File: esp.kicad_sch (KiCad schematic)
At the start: 26 parts, among them J1 Barrel_Jack, J3 Barrel_Jack, J4 Barrel_Jack, J5 Barrel_Jack, J7 Barrel_Jack_MountingPin, P1 Conn_WallPlug_Earth, U1 ESP32-S2-WROVER, U14 PCF8574ATS, U16 L298N, U17 PCA9685PW, U18 NID30S48-24, U2 TCA9548ARGER, U3 TCA9548ARGER, U4 BME280, U5 CCS811, U6 PCF8574ATS, U7 OKI-78SR-12_1.0-W36H-C, U8 OKI-78SR-5_1.5-W36-C, U9 OKI-78SR-3.3_1.5-W36H-C

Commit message: motor layout
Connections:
- net GND: no longer U3.9 (GND)
- net at U3.22 (A0): no longer U3.23 (A1)
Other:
- moved on the sheet: U14, U17, U3, U6
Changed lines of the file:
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@@
   (junction (at 66.04 30.48) (diameter 0) (color 0 0 0 0)
   )
-  (junction (at 44.45 88.9) (diameter 0) (color 0 0 0 0)
-  )
   (junction (at 267.97 60.96) (diameter 0) (color 0 0 0 0)
   )
@@
     (stroke (width 0) (type default))
   )
-  (wire (pts (xy 82.55 62.23) (xy 85.09 62.23))
-    (stroke (width 0) (type default))
-  )
   (wire (pts (xy 196.85 24.13) (xy 196.85 36.83))
     (stroke (width 0) (type default))
@@
     (stroke (width 0) (type default))
   )
-  (wire (pts (xy 31.75 88.9) (xy 31.75 102.87))
-    (stroke (width 0) (type default))
-  )
-  (wire (pts (xy 31.75 88.9) (xy 44.45 88.9))
-    (stroke (width 0) (type default))
-  )
   (wire (pts (xy 31.75 168.91) (xy 25.4 168.91))
     (stroke (width 0) (type default))
@@
     (stroke (width 0) (type default))
   )
-  (wire (pts (xy 69.85 72.39) (xy 44.45 72.39))
-    (stroke (width 0) (type default))
-  )
   (wire (pts (xy 162.56 50.8) (xy 173.99 50.8))
     (stroke (width 0) (type default))
@@
     (stroke (width 0) (type default))
   )
-  (wire (pts (xy 44.45 72.39) (xy 44.45 88.9))
-    (stroke (width 0) (type default))
-  )
   (wire (pts (xy 267.97 71.12) (xy 267.97 78.74))
     (stroke (width 0) (type default))
@@
     (stroke (width 0) (type default))
   )
-  (wire (pts (xy 110.49 62.23) (xy 110.49 54.61))
-    (stroke (width 0) (type default))
-  )
   (wire (pts (xy 27.94 25.4) (xy 33.02 25.4))
     (stroke (width 0) (type default))
@@
   )
   (wire (pts (xy 53.34 25.4) (xy 54.61 25.4))
-    (stroke (width 0) (type default))
-  )
-  (wire (pts (xy 113.03 62.23) (xy 113.03 57.15))
     (stroke (width 0) (type default))
   )
@@
     )
   )
-  (symbol (lib_id "Driver_LED:PCA9685PW") (at 99.06 132.08 180) (unit 1)
-    (in_bom yes) (on_board yes) (dnp no) (fields_autoplaced)
-    (property "Reference" "U17" (at 99.4059 104.14 0)
-      (effects (font (size 1.27 1.27)) (justify right))
-    )
-    (property "Value" "PCA9685PW" (at 99.4059 106.68 0)
-      (effects (font (size 1.27 1.27)) (justify right))
-    )
-    (property "Footprint" "Package_SO:TSSOP-28_4.4x9.7mm_P0.65mm" (at 98.425 107.315 0)
+  (symbol (lib_id "Driver_LED:PCA9685PW") (at 123.19 146.05 180) (unit 1)
+    (in_bom yes) (on_board yes) (dnp no) (fields_autoplaced)
+    (property "Reference" "U17" (at 123.5359 118.11 0)
+      (effects (font (size 1.27 1.27)) (justify right))
+    )
+    (property "Value" "PCA9685PW" (at 123.5359 120.65 0)
+      (effects (font (size 1.27 1.27)) (justify right))
+    )
+    (property "Footprint" "Package_SO:TSSOP-28_4.4x9.7mm_P0.65mm" (at 122.555 121.285 0)
       (effects (font (size 1.27 1.27)) (justify left) hide)
     )
-    (property "Datasheet" "http://www.nxp.com/docs/en/data-sheet/PCA9685.pdf" (at 109.22 149.86 0)
+    (property "Datasheet" "http://www.nxp.com/docs/en/data-sheet/PCA9685.pdf" (at 133.35 163.83 0)
       (effects (font (size 1.27 1.27)) hide)
     )
@@
     )
   )
-  (symbol (lib_id "Interface_Expansion:TCA9548ARGER") (at 95.25 72.39 270) (unit 1)
-    (in_bom yes) (on_board yes) (dnp no) (fields_autoplaced)
-    (property "Reference" "U3" (at 124.46 65.4619 90)
-      (effects (font (size 1.27 1.27)))
-    )
-    (property "Value" "TCA9548ARGER" (at 124.46 68.0019 90)
-      (effects (font (size 1.27 1.27)))
-    )
-    (property "Footprint" "Package_DFN_QFN:Texas_RGE0024C_EP2.1x2.1mm" (at 69.85 72.39 0)
-      (effects (font (size 1.27 1.27)) hide)
-    )
-    (property "Datasheet" "http://www.ti.com/lit/ds/symlink/tca9548a.pdf" (at 101.6 73.66 0)
+  (symbol (lib_id "Interface_Expansion:TCA9548ARGER") (at 162.56 138.43 180) (unit 1)
+    (in_bom yes) (on_board yes) (dnp no) (fields_autoplaced)
+    (property "Reference" "U3" (at 162.9059 110.49 0)
+      (effects (font (size 1.27 1.27)) (justify right))
+    )
+    (property "Value" "TCA9548ARGER" (at 162.9059 113.03 0)
+      (effects (font (size 1.27 1.27)) (justify right))
+    )
+    (property "Footprint" "Package_DFN_QFN:Texas_RGE0024C_EP2.1x2.1mm" (at 162.56 113.03 0)
+      (effects (font (size 1.27 1.27)) hide)
+    )
+    (property "Datasheet" "http://www.ti.com/lit/ds/symlink/tca9548a.pdf" (at 161.29 144.78 0)
       (effects (font (size 1.27 1.27)) hide)
     )
@@
     )
   )
-  (symbol (lib_id "power:GND") (at 44.45 88.9 0) (unit 1)
-    (in_bom yes) (on_board yes) (dnp no) (fields_autoplaced)
-    (property "Reference" "#PWR02" (at 44.45 95.25 0)
-      (effects (font (size 1.27 1.27)) hide)
-    )
-    (property "Value" "GND" (at 44.45 93.98 0)
-      (effects (font (size 1.27 1.27)))
-    )
-    (property "Footprint" "" (at 44.45 88.9 0)
-      (effects (font (size 1.27 1.27)) hide)
-    )
-    (property "Datasheet" "" (at 44.45 88.9 0)
-      (effects (font (size 1.27 1.27)) hide)
-    )
-    (pin "1")
-    (instances
-      (project "esp"
-        (path "/dab6683c-420f-459a-bf9c-0c28b4b081e3"
-          (reference "#PWR02") (unit 1)
-        )
-      )
-    )
-  )
   (symbol (lib_id "Connector:Conn_WallPlug_Earth") (at 20.32 27.94 0) (unit 1)
     (in_bom yes) (on_board yes) (dnp no) (fields_autoplaced)
@@
     )
   )
-  (symbol (lib_id "Interface_Expansion:PCF8574ATS") (at 100.33 179.07 180) (unit 1)
-    (in_bom yes) (on_board yes) (dnp no) (fields_autoplaced)
-    (property "Reference" "U6" (at 100.6759 158.75 0)
-      (effects (font (size 1.27 1.27)) (justify right))
-    )
-    (property "Value" "PCF8574ATS" (at 100.6759 161.29 0)
-      (effects (font (size 1.27 1.27)) (justify right))
-    )
-    (property "Footprint" "Package_SO:SSOP-20_4.4x6.5mm_P0.65mm" (at 100.33 179.07 0)
-      (effects (font (size 1.27 1.27)) hide)
-    )
-    (property "Datasheet" "http://www.nxp.com/docs/en/data-sheet/PCF8574_PCF8574A.pdf" (at 100.33 179.07 0)
+  (symbol (lib_id "Interface_Expansion:PCF8574ATS") (at 90.17 172.72 180) (unit 1)
+    (in_bom yes) (on_board yes) (dnp no) (fields_autoplaced)
+    (property "Reference" "U6" (at 90.5159 152.4 0)
+      (effects (font (size 1.27 1.27)) (justify right))
+    )
+    (property "Value" "PCF8574ATS" (at 90.5159 154.94 0)
+      (effects (font (size 1.27 1.27)) (justify right))
+    )
+    (property "Footprint" "Package_SO:SSOP-20_4.4x6.5mm_P0.65mm" (at 90.17 172.72 0)
+      (effects (font (size 1.27 1.27)) hide)
+    )
+    (property "Datasheet" "http://www.nxp.com/docs/en/data-sheet/PCF8574_PCF8574A.pdf" (at 90.17 172.72 0)
       (effects (font (size 1.27 1.27)) hide)
     )
@@
     )
   )
-  (symbol (lib_id "Interface_Expansion:PCF8574ATS") (at 63.5 106.68 180) (unit 1)
-    (in_bom yes) (on_board yes) (dnp no) (fields_autoplaced)
-    (property "Reference" "U14" (at 63.8459 86.36 0)
-      (effects (font (size 1.27 1.27)) (justify right))
-    )
-    (property "Value" "PCF8574ATS" (at 63.8459 88.9 0)
-      (effects (font (size 1.27 1.27)) (justify right))
-    )
-    (property "Footprint" "Package_SO:SSOP-20_4.4x6.5mm_P0.65mm" (at 63.5 106.68 0)
-      (effects (font (size 1.27 1.27)) hide)
-    )
-    (property "Datasheet" "http://www.nxp.com/docs/en/data-sheet/PCF8574_PCF8574A.pdf" (at 63.5 106.68 0)
+  (symbol (lib_id "Interface_Expansion:PCF8574ATS") (at 60.96 121.92 180) (unit 1)
+    (in_bom yes) (on_board yes) (dnp no) (fields_autoplaced)
+    (property "Reference" "U14" (at 61.3059 101.6 0)
+      (effects (font (size 1.27 1.27)) (justify right))
+    )
+    (property "Value" "PCF8574ATS" (at 61.3059 104.14 0)
+      (effects (font (size 1.27 1.27)) (justify right))
+    )
+    (property "Footprint" "Package_SO:SSOP-20_4.4x6.5mm_P0.65mm" (at 60.96 121.92 0)
+      (effects (font (size 1.27 1.27)) hide)
+    )
+    (property "Datasheet" "http://www.nxp.com/docs/en/data-sheet/PCF8574_PCF8574A.pdf" (at 60.96 121.92 0)
       (effects (font (size 1.27 1.27)) hide)
     )
@@
     )
   )
-  (sheet (at 12.7 148.59) (size 40.64 38.1) (fields_autoplaced)
+  (sheet (at 12.7 148.59) (size 149.86 48.26) (fields_autoplaced)
     (stroke (width 0.1524) (type solid))
     (fill (color 0 0 0 0.0000))
@@
       (effects (font (size 1.27 1.27)) (justify left bottom))
     )
-    (property "Sheetfile" "Barrel_Jack_Large_Motor.kicad_sch" (at 12.7 187.2746 0)
+    (property "Sheetfile" "Barrel_Jack_Large_Motor.kicad_sch" (at 12.7 197.4346 0)
       (effects (font (size 1.27 1.27)) (justify left top))
     )
@@
     )
   )
-  (sheet (at 19.05 104.14) (size 26.67 35.56) (fields_autoplaced)
+  (sheet (at 17.78 99.06) (size 144.78 44.45) (fields_autoplaced)
     (stroke (width 0.1524) (type solid))
     (fill (color 0 0 0 0.0000))
-    (property "Sheetname" "Barrel_Jack" (at 19.05 103.4284 0)
+    (property "Sheetname" "Barrel_Jack" (at 17.78 98.3484 0)
       (effects (font (size 1.27 1.27)) (justify left bottom))
     )
-    (property "Sheetfile" "Barrel_Jack.kicad_sch" (at 19.05 140.2846 0)
+    (property "Sheetfile" "Barrel_Jack.kicad_sch" (at 17.78 144.0946 0)
       (effects (font (size 1.27 1.27)) (justify left top))
     )

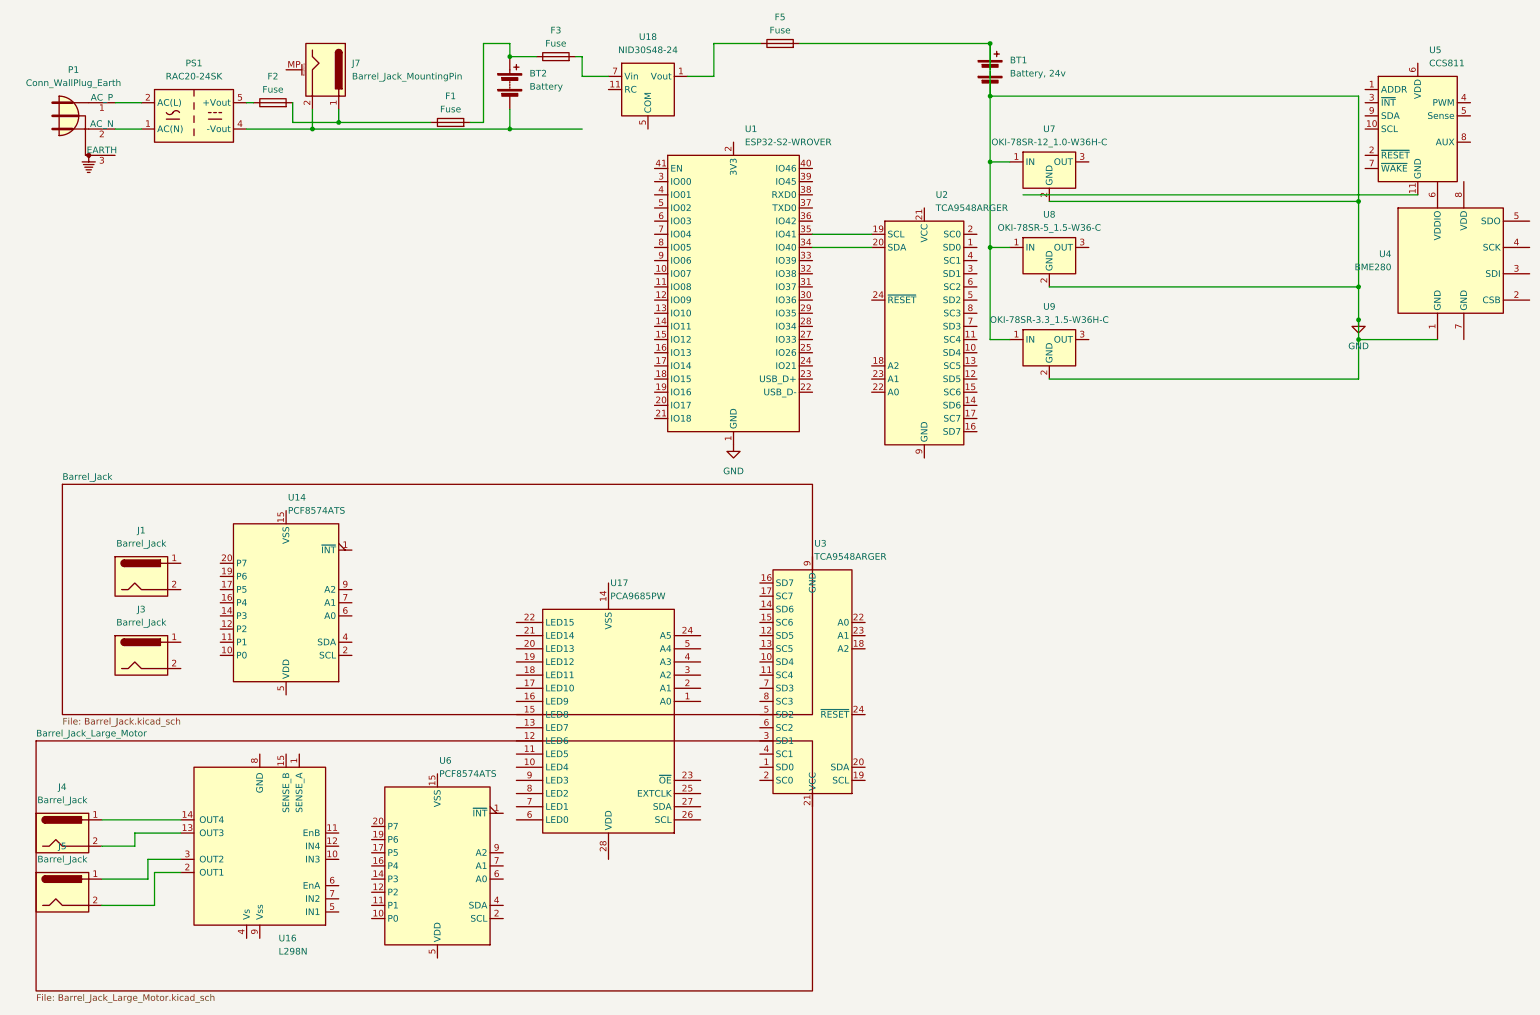
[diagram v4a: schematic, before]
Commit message: placeholders for ethernet and relay inputs
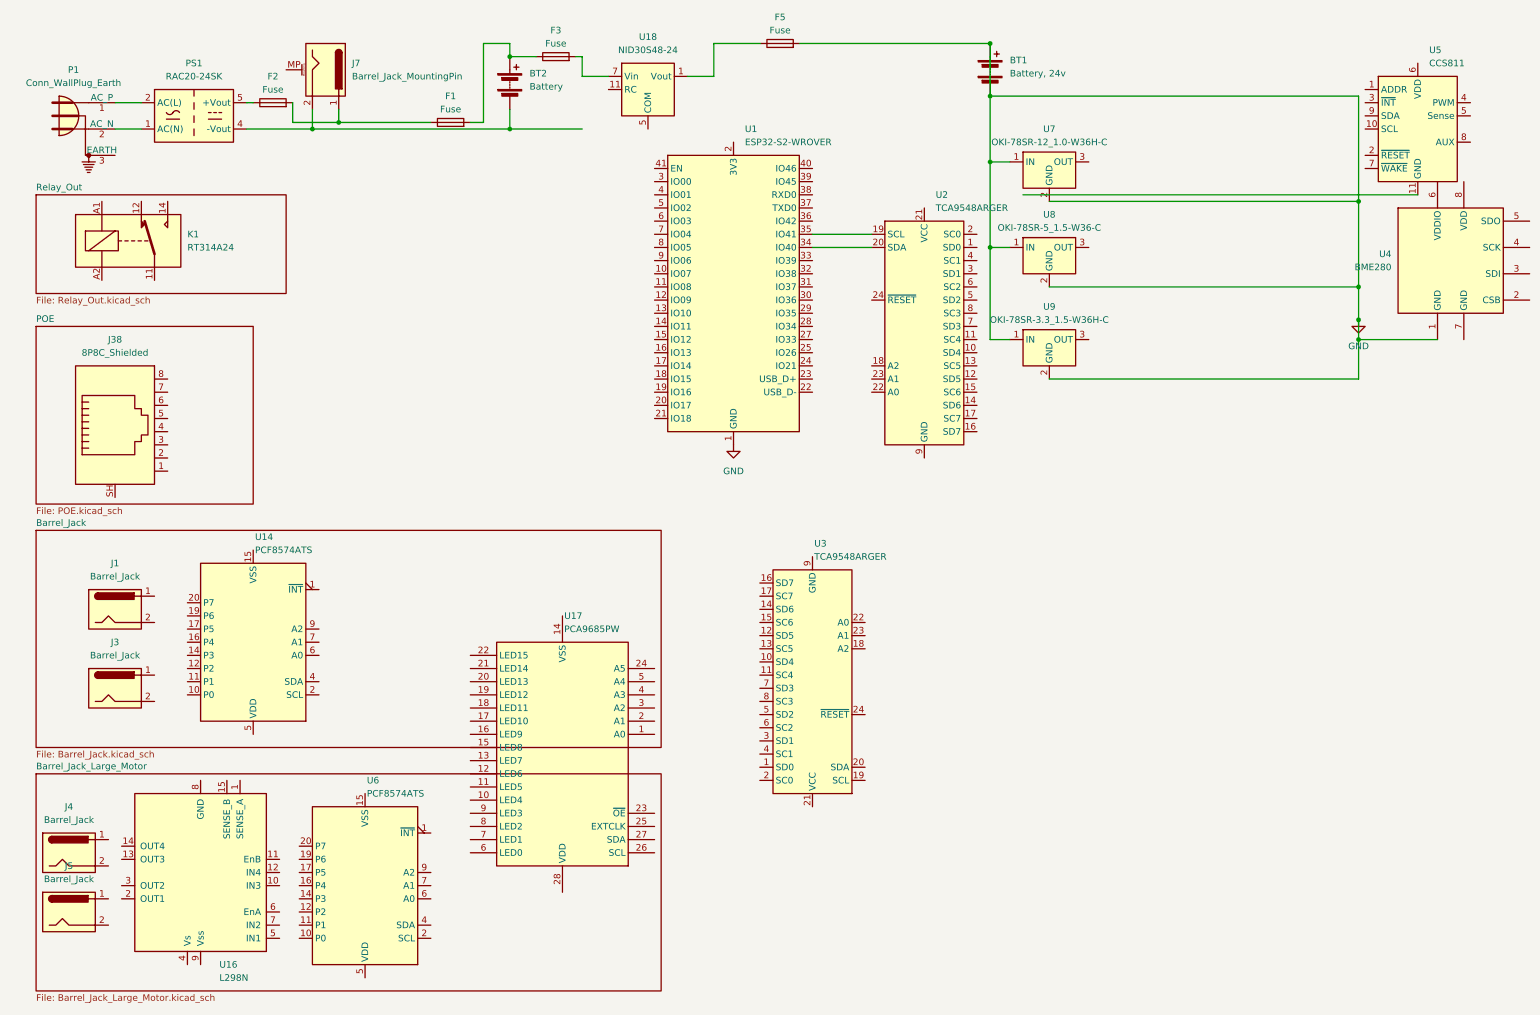
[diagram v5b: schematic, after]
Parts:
- added J38: 8P8C_Shielded, Connector_RJ:RJ45_HALO_HFJ11-x2450HRL_Horizontal, symbol Connector:8P8C_Shielded
- added K1: RT314A24, Relay_THT:Relay_1P1T_NO_10x24x18.8mm_Panasonic_ADW11xxxxW_THT, symbol Relay:RT314A24
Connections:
- net at J5.1: no longer U16.3 (OUT2)
- net at J5.2: no longer U16.2 (OUT1)
- net at J4.1: no longer U16.14 (OUT4)
- net at J4.2: no longer U16.13 (OUT3)
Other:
- added sheet POE (POE.kicad_sch)
- added sheet Relay_Out (Relay_Out.kicad_sch)
- moved on the sheet: J1, J3, J4, J5, U14, U16, U17, U6
